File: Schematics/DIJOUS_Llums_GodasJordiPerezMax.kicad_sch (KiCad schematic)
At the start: 67 parts, among them J1 Conn_01x05_Socket, J10 Screw_Terminal_01x02, J11 Conn_01x06, J5 Conn_01x05, J6 Conn_01x03, J7 Conn_01x02, J8 DE9_Plug, J9 Conn_01x06_Socket, K1 G5LE-1 DC12, Q1 ZXTN19020DFFTA, Q2 ZXTN19020DFFTA, Q3 Si7336ADP, Q4 Si7336ADP, Q5 ZXTN19020DFFTA, Q6 ZXTN19020DFFTA, Q7 Si7336ADP, Q8 Si7336ADP, Q9 ZXTN19020DFFTA, U2 LM2596T-ADJ, U3 PIC18F2580-I/SO, U4 MCP2551-I-SN, U5 ADP7112ACBZ-3.3-R7, U6 ADM7172ACPZ-5.0-R7, U7 PCA9306D

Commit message: Update DIJOUS_Llums_GodasJordiPerezMax.kicad_pro
update after class
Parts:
- removed C10: 2.2uF, symbol Device:C
- removed Q1: ZXTN19020DFFTA, symbol ZXTN:ZXTN19020DFFTA
- added C7: 100nF, symbol Device:C
- added Q10: ZXTN19020DFFTA, symbol ZXTN:ZXTN19020DFFTA
- added R20, R21, R22, R23: 100, symbol Device:R
- C8: value 100nF -> 2.2uF
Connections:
- net +3.3V_sensor is gone; now on net +3.3V: C1.1, C11.1, C3.2, J11.5 (Pin_5), J11.6 (Pin_6), R1.2, R2.2, U5.A2 (VOUT), U5.B2 (SENSE), U7.2 (VREF1)
- net +Vcc: no longer C15.1, C16.1, C8.1, J8.9, R14.1, R4.2, R6.2, R7.2, U4.3 (VDD), U5.A1 (VIN), U6.1 (VOUT), U6.2 (VOUT), U6.3 (SENSE)
- net Blinkers: now also Q5.2
- net Daytime lights: now also Q10.2; no longer Q5.2
- net GND: now also U5.C2 (GND), C7.2; no longer J8.6
- net GNDPWR: now also R21.2; no longer R17.2, U5.C2 (GND)
- net RA0: now also R17.1; no longer Q2.1
- net RA1: now also R16.1, R23.1; no longer R17.1
- net RA2: now also R21.1, R22.1; no longer Q5.1, R16.1
- net RA3: now also R20.1; no longer Q9.1
- net fuse_node: now reaches F1.1, J10.2 (Pin_2)
- net +3.3V: now reaches C5.2, U7.7 (VREF2)
- net +3.3V: no longer R7.1, U7.8 (EN)
- net VBAT renamed +12V
- net +12V: now also R7.1, Q10.3; no longer U5.C1 (EN)
- new net: Q10.1, R22.2
- new net: Q5.1, R23.2
- new net: Q9.1, R20.2
- new net: R7.2, U7.8 (EN)
- new net: Q2.1, R17.2
- new net +5V: C15.1, C16.1, C7.1, C8.1, R14.1, R4.2, R6.2, U4.3 (VDD), U5.A1 (VIN), U5.C1 (EN), U6.1 (VOUT), U6.2 (VOUT), U6.3 (SENSE)
- no-connect marks 7 -> 9
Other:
- note added: "VBat"
- note added: "close to the transceiver"
- note removed: "Ib max = 1A"
- moved on the sheet: C11, C3, J1, J5, K1, Q2, Q6, Q9, R1, R18, R19, R2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

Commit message: Update DIJOUS_Llums_GodasJordiPerezMax.kicad_sch
Resistencias botones y update puente + shunt y alguna footprint
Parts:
- added D1, D2, D7, D8: D, symbol Device:D
- added R24, R25, R26, R27, R28, R29, R30, R31, R32, R33, R34: 1k, Resistor_SMD:R_1206_3216Metric, symbol Device:R
- added R36: R_Shunt, Resistor_SMD:R_Shunt_Vishay_WSK2512_6332Metric_T2.66mm, symbol Device:R_Shunt
- R1, R10, R11, R12, R13, R14, R16, R17, R18, R19, R2, R20, R21, R22, R23, R3, R4, R5, R6, R7, R8, R9: footprint (none) -> Resistor_SMD:R_1206_3216Metric
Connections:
- net +12V: now also D1.1 (K), D8.1 (K)
- net +Vcc: now also R30.1
- net GND: now also U6.9 (GND), R24.2, R25.2, R26.2, R27.2, R28.2, R29.2, R30.2, R31.2, R32.2, R33.2, R34.2; no longer J8.3
- net GNDPWR: now also R36.4; no longer Q4.1 (S), Q4.2 (S), Q4.3 (S), Q8.1 (S), Q8.2 (S), Q8.3 (S), U6.9 (GND)
- net MCLR: now also R29.1
- net Motor_o1: now also D1.2 (A), D2.1 (K)
- net Motor_o2: now also D7.1 (K), D8.2 (A)
- net PGC: now also R32.1
- net PGD: now also R31.1
- net RC0: now also R24.1
- net RC1: now also R25.1
- net RC2: now also R26.1
- net RC6: now also R27.1
- net RC7: now also R28.1
- net SCL: now also R33.1
- net SDA: now also R34.1
- net ShuntV-: now reaches U3.25 (RB4/KBI0/AN9)
- net ShuntV-: now also R36.3
- net RB5: now reaches U3.26 (RB5/KBI1/PGM)
- net RB5: now also R17.1, R18.1
- removed net RA0: R17.1, R18.1, U3.2 (RA0/AN0)
- new net ShuntV+: R36.2, U3.2 (RA0/AN0)
- new net Shunt_in: D2.2 (A), D7.2 (A), Q4.1 (S), Q4.2 (S), Q4.3 (S), Q8.1 (S), Q8.2 (S), Q8.3 (S), R36.1
- no-connect marks 9 -> 8
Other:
- note added: "Shunt Resistor"
- note added: "Splitting capacitor. Near Hall"
- note added: "Splitting capacitor. Near Sensor"
- note added: "Splitting capacitor. Near VREF1"
- note added: "Splitting capacitor. Near VREF2"
- note added: "Splitting capacitor. Near micro"
- note removed: "Splitting capacitor"
- moved on the sheet: J1, J5, Q3

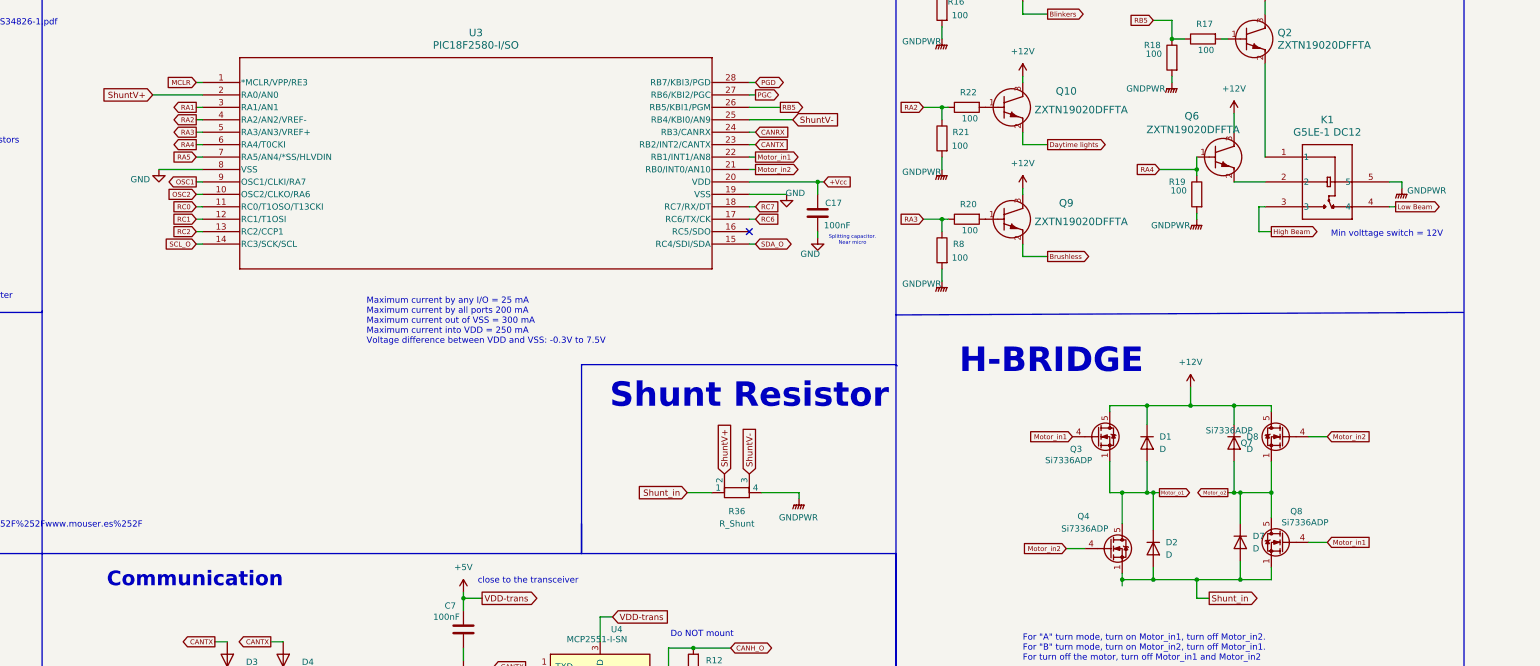
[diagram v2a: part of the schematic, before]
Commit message: Update DIJOUS_Llums_GodasJordiPerezMax.kicad_sch
Nueva actualización Puente H+ resistencia Shunt. Se han añadido bastantes huellas. Falta huellas restantes y la etapa Output select y se puede empezar Placement
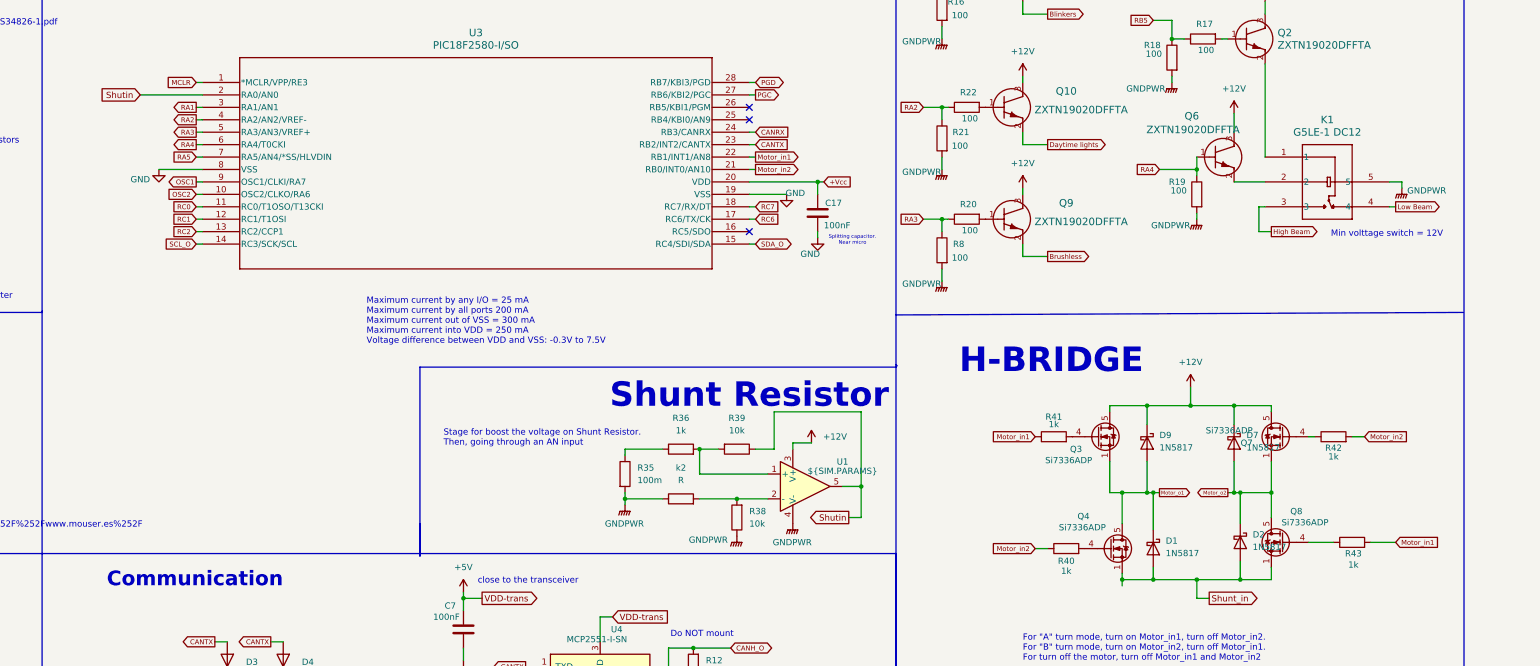
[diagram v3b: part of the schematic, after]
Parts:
- removed D1, D2, D7, D8: D, symbol Device:D
- removed R36: R_Shunt, Resistor_SMD:R_Shunt_Vishay_WSK2512_6332Metric_T2.66mm, symbol Device:R_Shunt
- added D1, D2, D7, D9: 1N5817, Diode_THT:D_DO-41_SOD81_P10.16mm_Horizontal, symbol Diode:1N5817
- added R35: 100m, Resistor_SMD:R_0402_1005Metric, symbol Device:R
- added R36, R40, R41, R42, R43: 1k, symbol Device:R
- added R38, R39: 10k, Resistor_SMD:R_0402_1005Metric, symbol Device:R
- added U1: ${SIM.PARAMS}, symbol Simulation_SPICE:OPAMP
- added k2: R, symbol Device:R
- C1, C11, C12, C13, C14, C15, C16, C17, C2, C3, C4, C5, C6, C7, C8, C9: footprint (none) -> Capacitor_SMD:C_1206_3216Metric_Pad1.33x1.80mm_HandSolder
- D3, D4: footprint (none) -> LED_SMD:LED_1206_3216Metric
- J1, J5: footprint (none) -> Connector_PinHeader_1.00mm:PinHeader_1x05_P1.00mm_Vertical
- J10: footprint (none) -> Connector_PinHeader_1.00mm:PinHeader_1x02_P1.00mm_Horizontal
- J11, J9: footprint (none) -> Connector_PinHeader_1.00mm:PinHeader_1x06_P1.00mm_Vertical
- J6: footprint (none) -> Connector_PinHeader_1.00mm:PinHeader_1x03_P1.00mm_Vertical
- J7: footprint (none) -> Connector_PinHeader_1.00mm:PinHeader_1x02_P1.00mm_Vertical
- L1: footprint (none) -> Inductor_SMD:L_Neosid_Ms42
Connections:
- net +12V: now also D7.1 (K), D9.1 (K), U1.3 (V+)
- net GNDPWR: now also R35.2, R38.1, U1.4 (V-), k2.1
- net Motor_in1: now also R41.1, R43.2; no longer Q3.4 (G), Q8.4 (G)
- net Motor_in2: now also R40.1, R42.2; no longer Q4.4 (G), Q7.4 (G)
- net Motor_o1: now also D1.1 (K), D9.2 (A)
- net Motor_o2: now also D2.1 (K), D7.2 (A)
- net RB5: no longer U3.26 (RB5/KBI1/PGM)
- net Shunt_in: now also D1.2 (A), D2.2 (A)
- net ShuntV+ renamed Shutin
- net Shutin: now also R39.1, U1.5
- net ShuntV-: no longer names the net of U3.25 (RB4/KBI0/AN9)
- new net: Q7.4 (G), R42.1
- new net: R35.1, R36.1
- new net: R38.2, U1.2 (-), k2.2
- new net: R36.2, R39.2, U1.1 (+)
- new net: Q8.4 (G), R43.1
- new net: Q3.4 (G), R41.2
- new net: Q4.4 (G), R40.2
- no-connect marks 8 -> 10
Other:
- note added: "Stage for boost the voltage on Shunt Resistor. Then, going through an AN input"

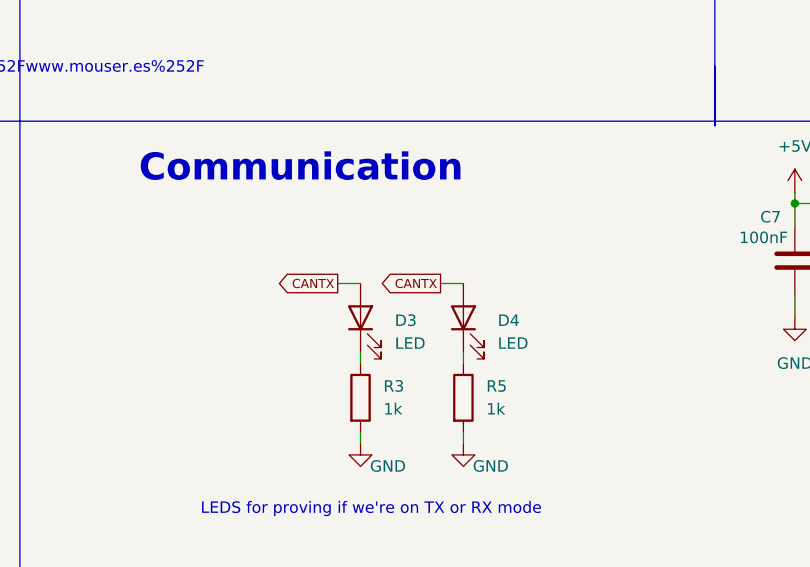
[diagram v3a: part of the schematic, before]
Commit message: Update DIJOUS_Llums_GodasJordiPerezMax.kicad_sch
Alguna pequeña corrección del esquemático. He añadido un par de huellas y cambiado algún pin que estaba mal. Faltan aún huellas por poner y alguna etapa por revisar (la del Hall y el Output select stage).
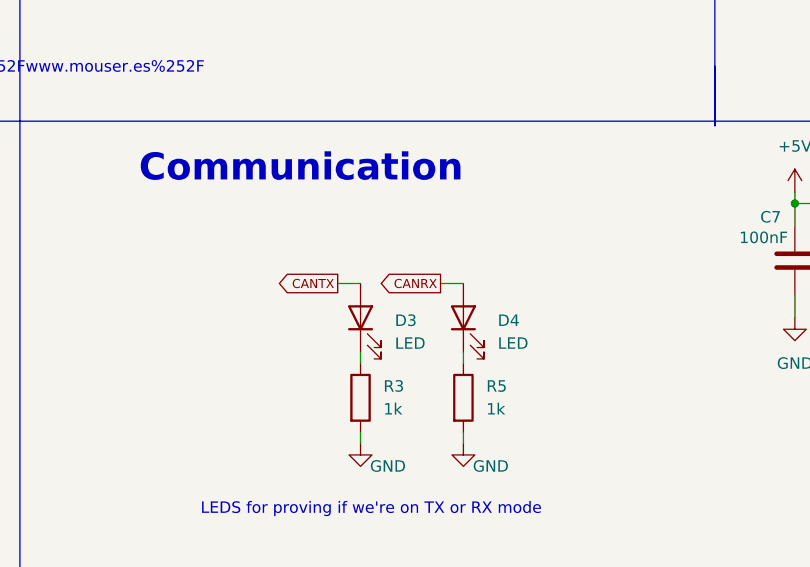
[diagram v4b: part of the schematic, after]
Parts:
- R12, R13: footprint Resistor_SMD:R_1206_3216Metric -> Resistor_THT:R_Axial_DIN0204_L3.6mm_D1.6mm_P5.08mm_Horizontal
- R40, R41, R42, R43: footprint (none) -> Resistor_SMD:R_1206_3216Metric
- U3: footprint (none) -> Package_SO:SOIC-28W_7.5x17.9mm_P1.27mm
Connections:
- net CANRX: now also D4.2 (A)
- net CANTX: no longer D4.2 (A)
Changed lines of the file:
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@@
 		)
 	)
-	(global_label "CANTX"
+	(global_label "CANRX"
 		(shape output)
 		(at 163.83 247.65 180)
@@
 		)
 		(property "Intersheetrefs" "${INTERSHEET_REFS}"
-			(at 156.2357 247.65 0)
+			(at 156.6226 247.65 0)
 			(effects
 				(font
@@
 			)
 		)
-		(property "Footprint" ""
+		(property "Footprint" "Resistor_SMD:R_1206_3216Metric"
 			(at 381 207.518 90)
 			(effects
@@
 			)
 		)
-		(property "Footprint" "Resistor_SMD:R_1206_3216Metric"
+		(property "Footprint" "Resistor_THT:R_Axial_DIN0204_L3.6mm_D1.6mm_P5.08mm_Horizontal"
 			(at 251.968 264.16 90)
 			(effects
@@
 			)
 		)
-		(property "Footprint" ""
+		(property "Footprint" "Package_SO:SOIC-28W_7.5x17.9mm_P1.27mm"
 			(at 149.86 133.35 0)
 			(effects
@@
 			)
 		)
-		(property "Footprint" ""
+		(property "Footprint" "Resistor_SMD:R_1206_3216Metric"
 			(at 326.39 230.378 90)
 			(effects
@@
 			)
 		)
-		(property "Footprint" ""
+		(property "Footprint" "Resistor_SMD:R_1206_3216Metric"
 			(at 384.81 229.108 90)
 			(effects
@@
 			)
 		)
-		(property "Footprint" "Resistor_SMD:R_1206_3216Metric"
+		(property "Footprint" "Resistor_THT:R_Axial_DIN0204_L3.6mm_D1.6mm_P5.08mm_Horizontal"
 			(at 251.968 252.73 90)
 			(effects
@@
 			)
 		)
-		(property "Footprint" ""
+		(property "Footprint" "Resistor_SMD:R_1206_3216Metric"
 			(at 323.85 207.518 90)
 			(effects

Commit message: Update DIJOUS_Llums_GodasJordiPerezMax.kicad_sch
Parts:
- removed C5: 100nF, Capacitor_SMD:C_1206_3216Metric_Pad1.33x1.80mm_HandSolder, symbol Device:C
- removed CR1: SS3P5HM3/84A, CR_5HM3/84A_VIS, symbol SS3P5:SS3P5HM3_84A
- removed Q2: ZXTN19020DFFTA, symbol ZXTN:ZXTN19020DFFTA
- removed R17, R18: 100, Resistor_SMD:R_1206_3216Metric, symbol Device:R
- removed U1: ${SIM.PARAMS}, symbol Simulation_SPICE:OPAMP
- added CR2: SS3P5HM3/84A, SS3P5:CR_5HM3&slash_84A_VIS, symbol SS3P5:SS3P5HM3_84A
- added K3: G5LE-1 DC12, G5LE-1-DC12:RELAY_G5LE-1 DC5_OMR, symbol G5LE-1-DC12:G5LE-1_DC12
- added Q1: ZXTN19020DFFTA, ZXTN:ZXTN19020DFFTA_DIO, symbol ZXTN:ZXTN19020DFFTA
- added R37: 100, Resistor_SMD:R_1206_3216Metric, symbol Device:R
- added U1: LT6202CS5, S_5_ADI, symbol LT6202CS5:LT6202CS5
- Q10, Q5, Q6, Q9: footprint (none) -> ZXTN:ZXTN19020DFFTA_DIO
- R36: footprint (none) -> Resistor_SMD:R_1206_3216Metric
- XTAL1: footprint XTAL_ANA8M_VIS -> XT9M20HRR8M:XTAL_ANA8M_VIS
- k2: value R -> 1k; footprint (none) -> Resistor_SMD:R_1206_3216Metric
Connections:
- net +12V: now also K1.1, K3.1, Q1.3, U1.5 (V+)
- net GND: now also J8.5; no longer U6.9 (GND)
- net GNDPWR: now also K1.4, U6.9 (GND), CR2.2, K3.4, K3.5, R37.2, U1.2 (V-)
- net Low Beam: now also K3.3; no longer K1.4
- net RA5: now also Q1.1, R37.1; no longer J6.1 (Pin_1), R14.2
- net RB5: now also J6.1 (Pin_1), R14.2, U3.26 (RB5/KBI1/PGM)
- net Shutin: now also U1.1 (OUT)
- net at L1.1, U2.2 (OUT): now also CR2.1
- net at R38.2, k2.2: now also U1.4 (-IN)
- net at R36.2, R39.2: now also U1.3 (+IN)
- new net: K3.2, Q1.2
- no-connect marks 10 -> 8
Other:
- note added: "RA5 sends a signal to the uc wich depending on the voltage recieved will know the position of the motor High state: 14.5mA * 220Ω = 3.19V Low state: 3.5 mA * 220Ω = 0.77V"
- note added: "Splitting capacitor. 2 Near VREF1 and VREF2"
- note added: "Unió dels dos GNDs"
- note removed: "RA5 sends a signal to the uc wich depending on the voltage recieved will know the position of the motor"
- note removed: "Splitting capacitor. Near VREF1"
- note removed: "Splitting capacitor. Near VREF2"
- moved on the sheet: C17, C3, D1, D2, D7, D9, J7, J8, J9, K1, Q10, Q3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
